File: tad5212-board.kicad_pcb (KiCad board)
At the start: 4 copper layers, 18.1 x 25.7 mm, 11 parts, among them J1 Conn_01x10, J2 Conn_01x10, U1 XTAD5212IRGER

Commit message: LICENSE
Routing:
- net GND: vias 7 -> 19
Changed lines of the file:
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@@
 		)
 		(pad_to_mask_clearance 0)
-		(solder_mask_min_width 0.12)
 		(allow_soldermask_bridges_in_footprints no)
 		(tenting front back)
@@
 			(plot_on_all_layers_selection 0x00000000_00000000_00000000_00000000)
 			(disableapertmacros no)
-			(usegerberextensions no)
+			(usegerberextensions yes)
 			(usegerberattributes yes)
 			(usegerberadvancedattributes yes)
-			(creategerberjobfile yes)
+			(creategerberjobfile no)
 			(dashed_line_dash_ratio 12.000000)
 			(dashed_line_gap_ratio 3.000000)
@@
 			(sketchdnponfab yes)
 			(crossoutdnponfab yes)
-			(subtractmaskfromsilk no)
+			(subtractmaskfromsilk yes)
 			(outputformat 1)
 			(mirror no)
-			(drillshape 1)
+			(drillshape 0)
 			(scaleselection 1)
-			(outputdirectory "")
+			(outputdirectory "gerbers/")
 		)
 	)
@@
 	)
 	(via
+		(at 144.8 73.2)
+		(size 0.6)
+		(drill 0.3)
+		(layers "F.Cu" "B.Cu")
+		(net 2)
+	)
+	(via
 		(at 142.3 70.4)
 		(size 0.6)
@@
 	)
 	(via
+		(at 145.5 73.9)
+		(size 0.6)
+		(drill 0.3)
+		(layers "F.Cu" "B.Cu")
+		(net 2)
+	)
+	(via
+		(at 144.1 73.9)
+		(size 0.6)
+		(drill 0.3)
+		(layers "F.Cu" "B.Cu")
+		(net 2)
+	)
+	(via
+		(at 144.8 73.2)
+		(size 0.6)
+		(drill 0.3)
+		(layers "F.Cu" "B.Cu")
+		(net 2)
+	)
+	(via
 		(at 147.7 71)
 		(size 0.6)
@@
 	)
 	(via
+		(at 144.8 73.2)
+		(size 0.6)
+		(drill 0.3)
+		(layers "F.Cu" "B.Cu")
+		(net 2)
+	)
+	(via
 		(at 142.7 78.7)
 		(size 0.6)
@@
 	)
 	(via
+		(at 145.5 72.5)
+		(size 0.6)
+		(drill 0.3)
+		(layers "F.Cu" "B.Cu")
+		(net 2)
+	)
+	(via
+		(at 144.1 72.5)
+		(size 0.6)
+		(drill 0.3)
+		(layers "F.Cu" "B.Cu")
+		(net 2)
+	)
+	(via
+		(at 145.5 73.9)
+		(size 0.6)
+		(drill 0.3)
+		(layers "F.Cu" "B.Cu")
+		(net 2)
+	)
+	(via
+		(at 144.8 73.2)
+		(size 0.6)
+		(drill 0.3)
+		(layers "F.Cu" "B.Cu")
+		(net 2)
+	)
+	(via
+		(at 144.8 73.2)
+		(size 0.6)
+		(drill 0.3)
+		(layers "F.Cu" "B.Cu")
+		(net 2)
+	)
+	(via
 		(at 141.2 78.8)
 		(size 0.6)
@@
 		(size 0.6)
 		(drill 0.3)
+		(layers "F.Cu" "B.Cu")
+		(net 2)
+	)
+	(via
+		(at 144.8 73.2)
+		(size 0.6)
+		(drill 0.3)
+		(layers "F.Cu" "B.Cu")
+		(net 2)
+	)
+	(via
+		(at 144.8 73.2)
+		(size 0.6)
+		(drill 0.3)

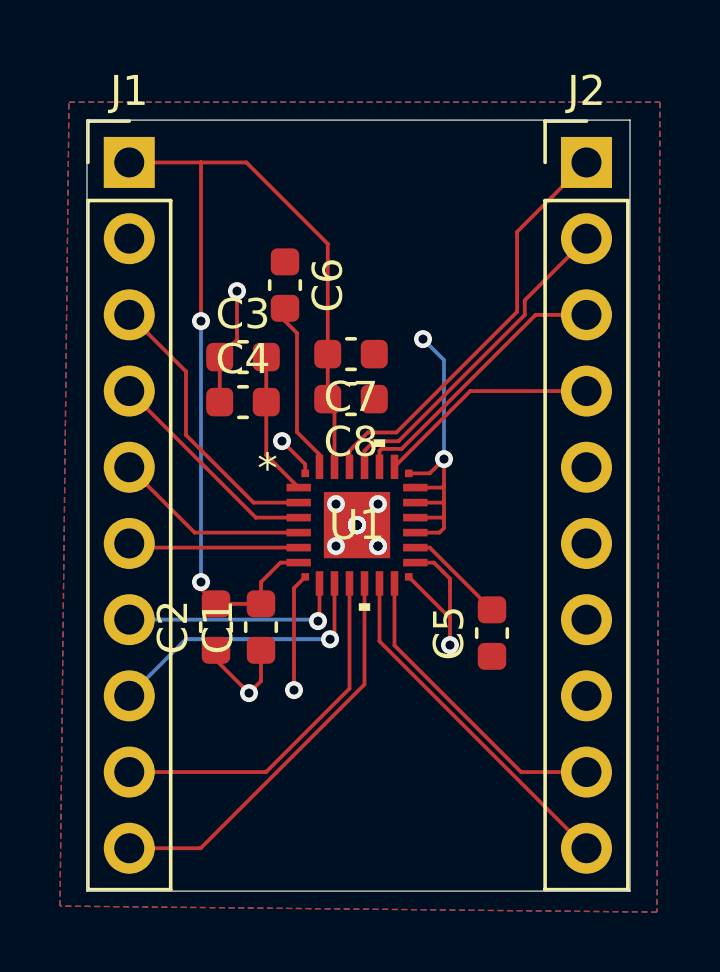
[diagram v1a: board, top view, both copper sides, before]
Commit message: v2 with hive compat footprints and fix i2c
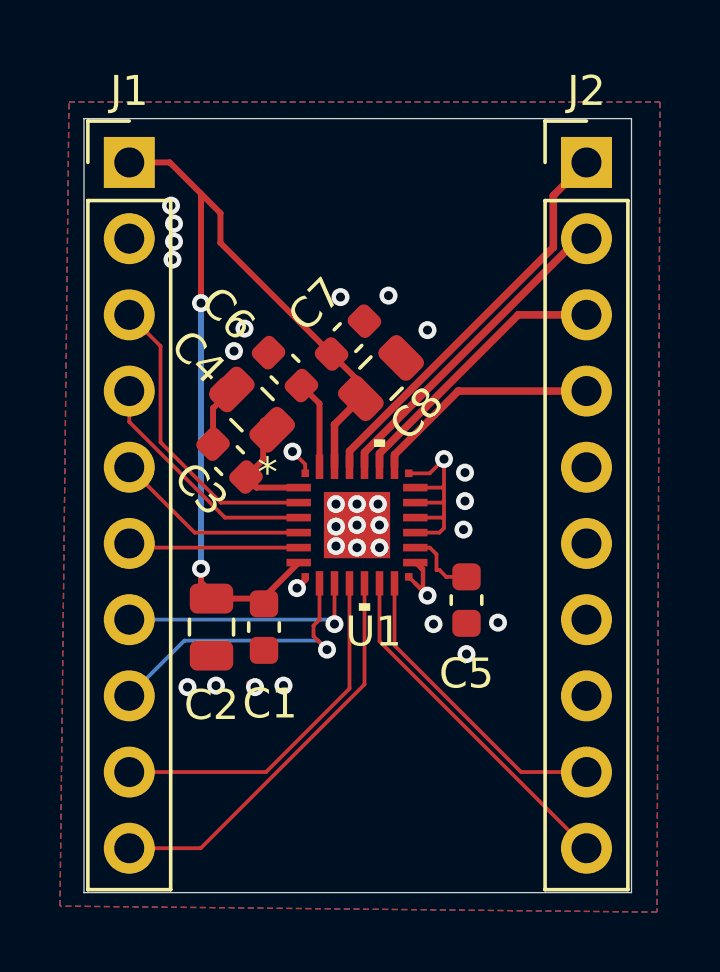
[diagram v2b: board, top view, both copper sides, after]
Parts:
- C1, C3, C7: value 0.1uF -> 100nF
- C2, C4, C8: footprint Capacitor_SMD:C_0603_1608Metric -> Capacitor_SMD:C_0805_2012Metric
- moved C3 3.48 mm to (140.6, 71.0), turned to -45 degrees
- moved C6 2.80 mm to (142.4, 68.0), turned to -45 degrees
- moved C5 1.39 mm to (148.4, 75.7)
- moved C8 1.22 mm to (145.6, 68.3), turned to -135 degrees
- moved C7 0.56 mm to (144.5, 67.0), turned to -135 degrees
- moved C4 0.39 mm to (141.3, 69.3), turned to -45 degrees
- moved C2 0.15 mm to (139.9, 76.6)
- moved C1 0.10 mm to (141.7, 76.6)
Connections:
- U1 pad 7: /SDA -> /SCL
- U1 pad 8: /SCL -> /SDA
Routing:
- net GND: track 30.2 -> 14.4 mm, vias 19 -> 32
- net Net-(U1-VREF): track 5.76 -> 2.96 mm
- net Net-(U1-MICBIAS): track 3.42 -> 2.42 mm
- net +3.3V: track 33.9 -> 33.0 mm
- net /DREG: track 4.80 -> 4.02 mm
- net /SDA: track 7.59 -> 8.26 mm
- net /BCLK: track 9.48 -> 10.1 mm
- net /FSYNC: track 7.39 -> 8.00 mm
- net /OUT2M: track 14.0 -> 13.4 mm
- net /SCL: track 9.40 -> 9.95 mm
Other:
- board size 18.1 x 25.7 mm -> 18.2 x 25.8 mm
- copper layers 4 -> 2
- board text added: "TAD5212 Board v2 By Isaiah Gamble"
- board text removed: "TAD5212 Board By Isaiah Gamble"

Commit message: make 4-layer; add ldo
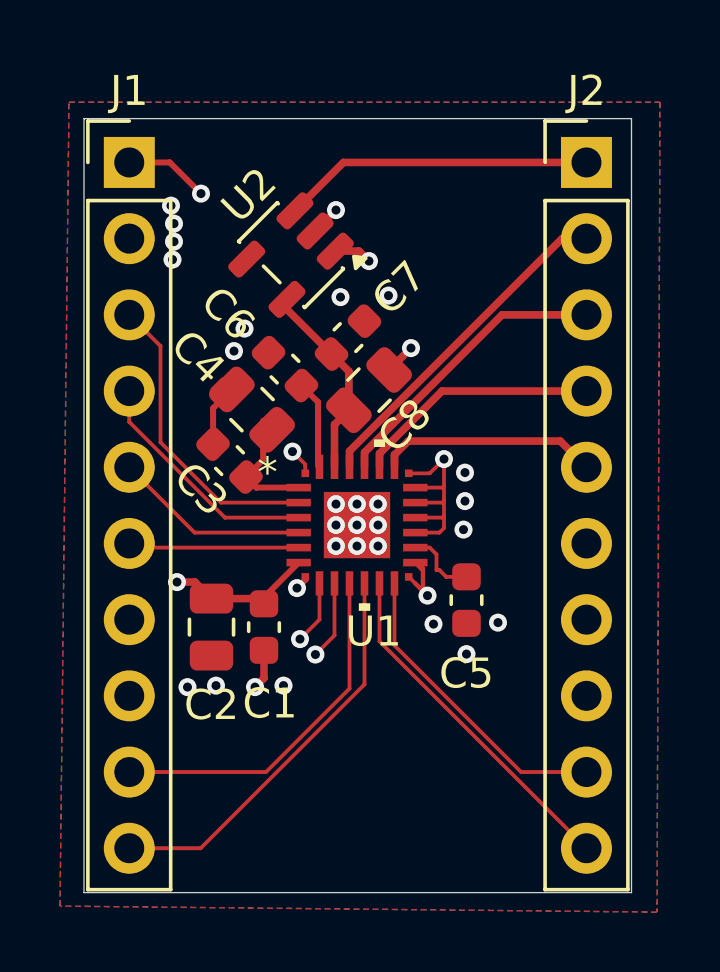
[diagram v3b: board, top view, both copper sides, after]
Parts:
- added REF**: ibomb, ibomb:ibomb, F.Cu at (146.1, 81.5)
- added U2: LP5907MFX-1.8, Package_TO_SOT_SMD:SOT-23-5, F.Cu at (142.6, 64.2)
- moved C8 0.57 mm to (145.2, 68.7)
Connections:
- C7 pad 2: +3.3V -> /AVDD
- C8 pad 2: +3.3V -> /AVDD
- J2 pad 1: /OUT2M -> /LDO_EN
- J2 pad 2: /OUT2P -> /OUT2M
- J2 pad 3: /OUT1P -> /OUT2P
- J2 pad 4: /OUT1M -> /OUT1P
- J2 pad 5: unconnected-(J2-Pin_5-Pad5) -> /OUT1M
- U1 pad 23: +3.3V -> /AVDD
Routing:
- net +3.3V: track 33.0 -> 9.42 mm, vias 2 -> 3
- net /LDO_EN: track 0.00 -> 10.4 mm
- net /AVDD: track 0.00 -> 6.51 mm
- net GND: track 14.4 -> 17.8 mm, vias 32 -> 33
- net /OUT2M: track 13.4 -> 11.6 mm
- net /SDA: track 8.26 -> 9.73 mm
- net /SCL: track 9.95 -> 8.60 mm
- net /OUT2P: track 11.1 -> 9.78 mm
- net /OUT1P: track 9.26 -> 8.20 mm
- added copper zone on In2.Cu, net +3.3V
- added copper zone on In1.Cu, net GND
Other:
- copper layers 2 -> 4
- board text added: "IBOMB"
- board text added: "TAD 5212"
- board text added: "TAD5212 v3 By Isaiah G"
- board text added: "ldo_en"
- board text removed: "TAD5212 Board v2 By Isaiah Gamble"

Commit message: add via stitching
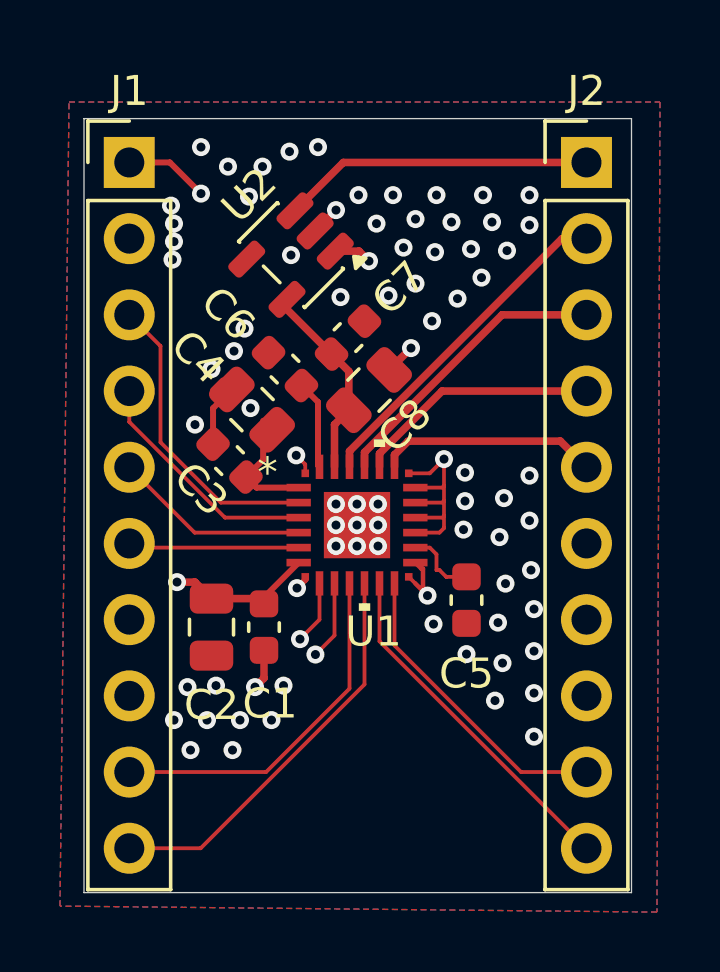
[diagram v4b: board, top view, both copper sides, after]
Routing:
- net GND: track 17.8 -> 17.7 mm, vias 33 -> 79

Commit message: add oscillator
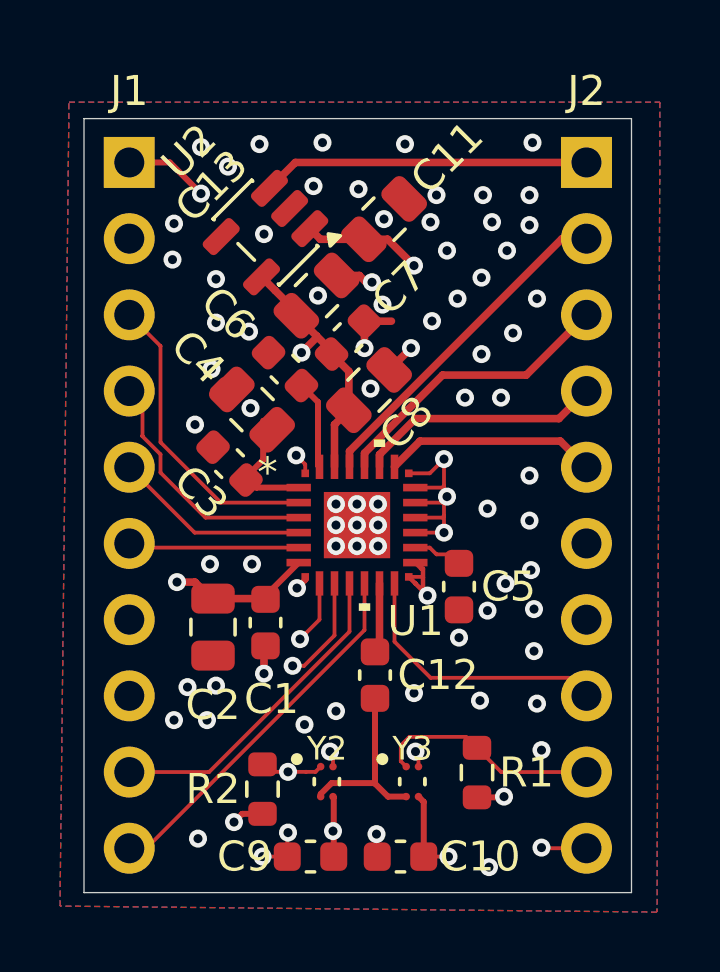
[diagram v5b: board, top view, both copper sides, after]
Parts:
- removed REF**: ibomb, ibomb:ibomb
- added C10: 10nF, Capacitor_SMD:C_0603_1608Metric, F.Cu at (146.2, 84.2)
- added C11: 10uF, Capacitor_SMD:C_0805_2012Metric, F.Cu at (145.7, 63.0)
- added C12: 13pF, Capacitor_SMD:C_0603_1608Metric, F.Cu at (145.4, 78.2)
- added C13: 10uF, Capacitor_SMD:C_0805_2012Metric, F.Cu at (143.4, 65.5)
- added C9: 10nF, Capacitor_SMD:C_0603_1608Metric, F.Cu at (143.2, 84.2)
- added G***: LOGO, LOGO, B.Cu at (144.4, 62.5)
- added R1: 10k, Resistor_SMD:R_0603_1608Metric, F.Cu at (148.8, 81.5)
- added R2: 10k, Resistor_SMD:R_0603_1608Metric, F.Cu at (141.7, 82.0)
- added Y2: SIT8021AI-J4-XXS-11.1E, SIT8021AI-J4-XXS-24.000000E:OSC_SIT8021AI-J4-XXS-24.000000E, F.Cu at (143.8, 81.8)
- added Y3: SIT8021AI-J4-XXS-12.288E, SIT8021AI-J4-XXS-24.000000E:OSC_SIT8021AI-J4-XXS-24.000000E, F.Cu at (146.6, 81.8)
- moved U2 1.13 mm to (141.8, 63.5)
- moved C5 0.51 mm to (148.2, 75.2)
- moved C1 0.16 mm to (141.8, 76.5)
- moved C3 0.10 mm to (140.6, 71.2)
- moved C2 0.05 mm to (140.0, 76.6)
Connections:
- net /AVDD renamed +1V8
- J2 pad 10: /GPO1 -> /DIS_CLK2
- J2 pad 8: unconnected-(J2-Pin_8-Pad8) -> /GPI1
- J2 pad 9: /GPI1 -> /DIS_CLK1
- U1 pad 11: /GPO1 -> Net-(U1-GPO1)
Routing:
- net +3.3V: track 9.42 -> 33.5 mm
- net /DIS_CLK2: track 0.00 -> 14.8 mm, vias 0 -> 2
- net +1V8: track 6.51 -> 15.6 mm, vias 0 -> 5
- net /DIS_CLK1: track 0.00 -> 7.74 mm
- net /GPO1: track 11.7 -> 6.03 mm
- net GND: track 17.7 -> 20.6 mm, vias 79 -> 84
- net Net-(U1-GPO1): track 0.00 -> 2.34 mm
- net /SDA: track 9.73 -> 11.3 mm
- net /GPI1: track 10.2 -> 9.09 mm
- net /GPIO1: track 12.0 -> 10.9 mm
- net /GPIO2: track 13.5 -> 12.5 mm
- net Net-(U1-MICBIAS): track 2.42 -> 1.67 mm
- net /LDO_EN: track 10.4 -> 10.9 mm
- added copper zone on In2.Cu, net +1V8
- removed copper zone on In2.Cu, net +3.3V
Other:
- board text added: "TAD5212 v4 (w/ external oscillators) By Isaiah Gamble"
- board text added: "dis_clk1"
- board text added: "dis_clk2"
- board text removed: "IBOMB"
- board text removed: "TAD 5212"
- board text removed: "TAD5212 v3 By Isaiah G"
- board text removed: "gpo1"
